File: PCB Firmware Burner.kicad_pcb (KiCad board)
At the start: 2 copper layers, 34.7 x 35.3 mm, 19 parts, among them J1 Conn_01x06_Male, Q1 BSS138, Q2 BSS138

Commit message: revision 1.1
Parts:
- removed CHC1: 100nF, Capacitor_SMD:C_1206_3216Metric
- removed the REF** at (159.0, 75.6)
- removed the REF** at (167.5, 75.5)
- added G***: LOGO, AeonLabs:aeon creative commons logos, F.Cu at (175.6, 99.8)
- added G***: LOGO, AeonLabs:aeon creative commons logos, B.Cu at (163.5, 98.1)
- added QR1: 10K, Resistor_SMD:R_0805_2012Metric_Pad1.20x1.40mm_HandSolder, F.Cu at (168.3, 88.8)
- added QR2: 10K, Resistor_SMD:R_0805_2012Metric_Pad1.20x1.40mm_HandSolder, F.Cu at (174.1, 90.6)
- added REF**: TestPoint_Plated_Hole_D2.0mm, TestPoint:TestPoint_Plated_Hole_D2.0mm, F.Cu at (160.7, 75.4)
- added REF**: TestPoint_Plated_Hole_D2.0mm, TestPoint:TestPoint_Plated_Hole_D2.0mm, F.Cu at (167.1, 75.5)
- moved Q2 2.60 mm to (176.9, 88.5)
- moved Q1 2.36 mm to (171.1, 88.0)
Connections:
- CH340K1 pad 4: Net-(Q2-Pad1) -> Net-(CH340K1-Pad4)
- CH340K1 pad 6: Net-(Q2-Pad2) -> Net-(CH340K1-Pad6)
- LDR1 pad 1: /CH3V3 -> /3V3
- Q1 pad 1: Net-(Q2-Pad2) -> Net-(Q1-Pad1)
- Q1 pad 2: Net-(Q2-Pad1) -> Net-(CH340K1-Pad4)
- Q2 pad 2: Net-(Q2-Pad2) -> Net-(CH340K1-Pad6)
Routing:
- net Net-(CH340K1-Pad6): track 0.00 -> 16.6 mm, vias 0 -> 4
- net Net-(Q2-Pad2): track 16.4 -> 0.00 mm, vias 3 -> 0
- net /GND: track 89.3 -> 78.2 mm
- net Net-(Q2-Pad1): track 10.8 -> 1.93 mm
- net Net-(CH340K1-Pad4): track 0.00 -> 8.34 mm
- net /RST_EN_RTS: track 15.8 -> 10.6 mm
- net Net-(Q1-Pad1): track 0.00 -> 2.31 mm
- net /IO0_BOOT_DTR: track 5.69 -> 6.94 mm
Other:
- board text added: "3V3"
- board text added: "Copyright 2022 rev. 1.1"
- board text removed: "Copyright 2022 rev. 1.0"

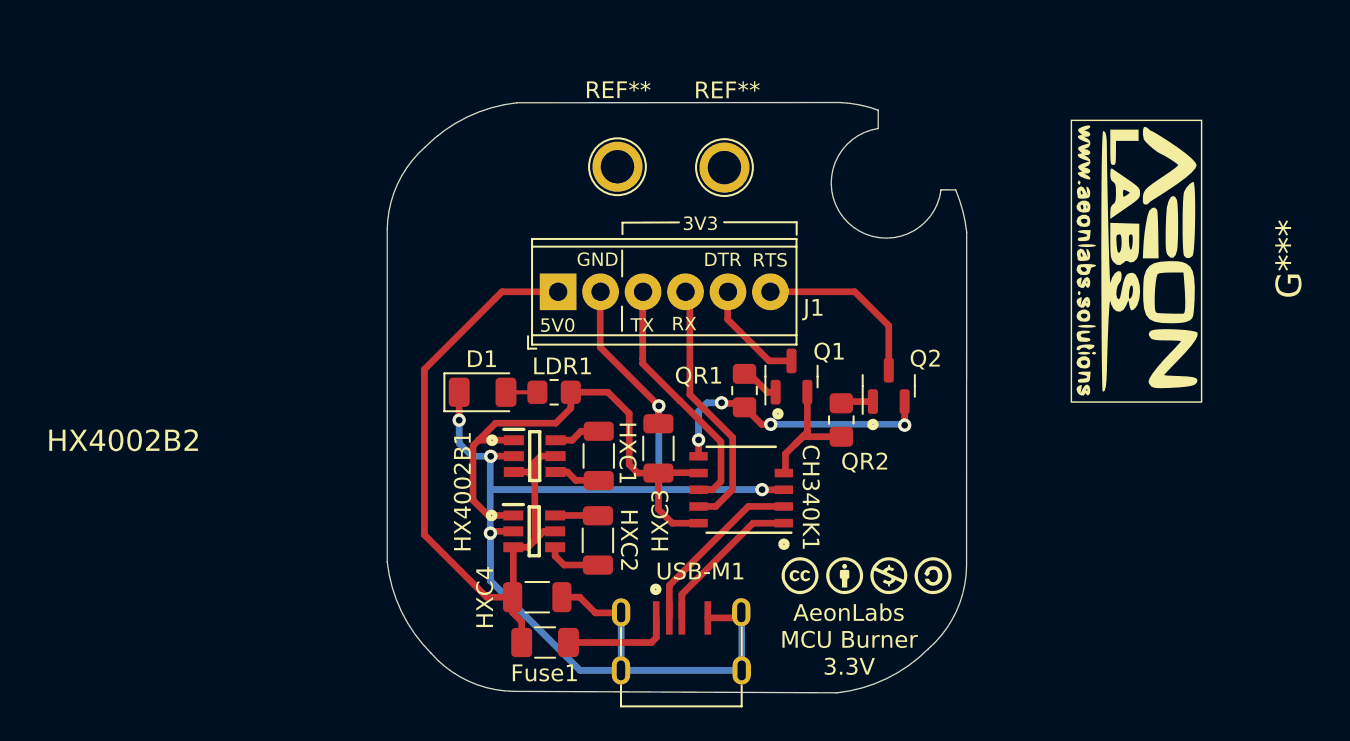
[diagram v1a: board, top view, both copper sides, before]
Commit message: revision 1.2
possibility of voltage selection: 3V3 or 5V0
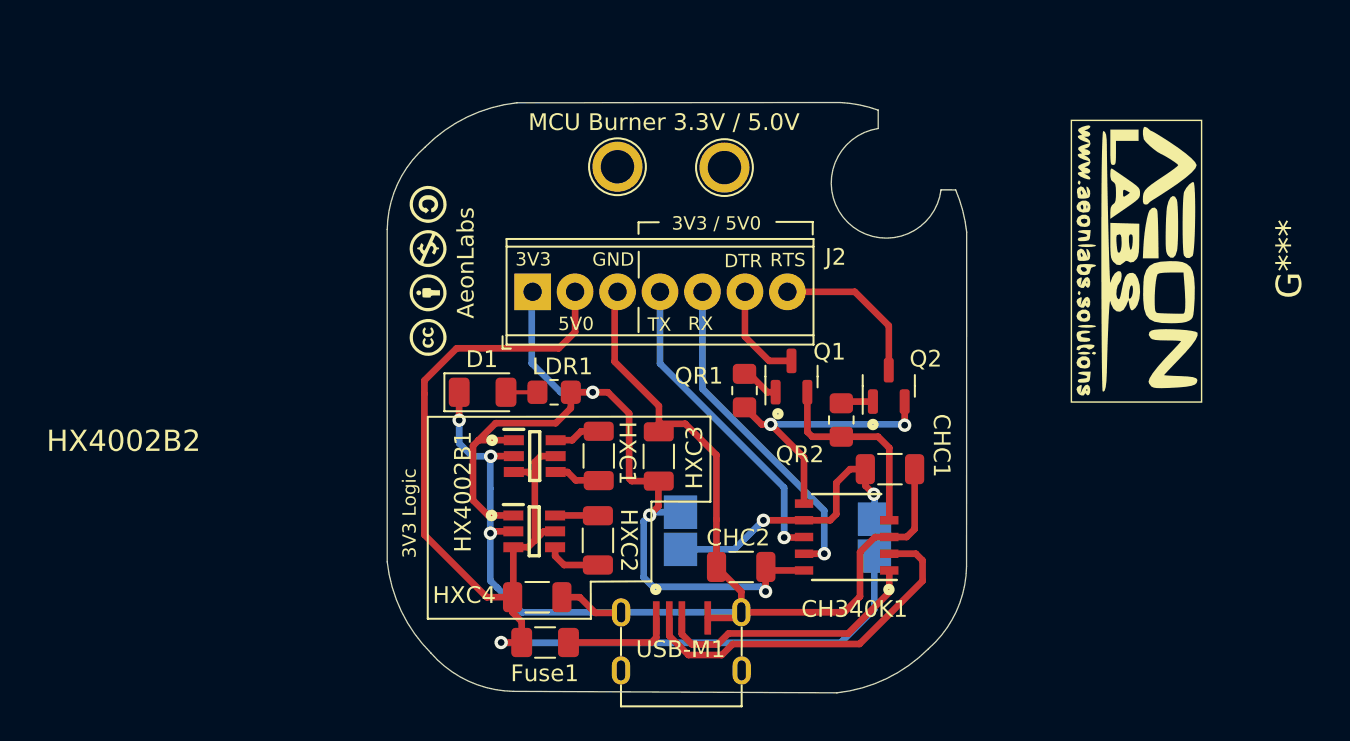
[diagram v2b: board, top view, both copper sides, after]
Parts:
- removed J1: Conn_01x06_Male, TerminalBlock_Phoenix:TerminalBlock_Phoenix_MPT-0,5-6-2.54_1x06_P2.54mm_Horizontal
- added CHC1: 100nF, Capacitor_SMD:C_1206_3216Metric, F.Cu at (177.0, 93.5)
- added CHC2: 100nF, Capacitor_SMD:C_1206_3216Metric, F.Cu at (168.1, 99.3)
- added J2: Conn_01x07_Male, TerminalBlock_Phoenix:TerminalBlock_Phoenix_MPT-0,5-7-2.54_1x07_P2.54mm_Horizontal, F.Cu at (155.6, 82.9)
- added T5V0b1: T5V0b1, TestPoint:TestPoint_Pad_2.0x2.0mm, B.Cu at (176.1, 98.7)
- added T5V0b2: T5V0b2, TestPoint:TestPoint_Pad_2.0x2.0mm, B.Cu at (164.5, 98.3)
- added T5V0c1: T5V0c1, TestPoint:TestPoint_Pad_2.0x2.0mm, B.Cu at (176.1, 96.5)
- added T5V0c2: T5V0c2, TestPoint:TestPoint_Pad_2.0x2.0mm, B.Cu at (164.5, 96.1)
- moved G*** 31.9 mm to (149.3, 81.7), turned to 90 degrees
- moved G*** 19.7 mm to (164.1, 78.4)
- moved CH340K1 6.91 mm to (174.4, 97.6)
- moved HXC3 0.48 mm to (163.2, 92.7)
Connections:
- CH340K1 pad 10: /CH3V3 -> /HX3V3
- CH340K1 pad 7: /CH3V3 -> Net-(CH340K1-Pad7)
- HX4002B1 pad 1: /CH3V3 -> /HX3V3
- HX4002B2 pad 1: /CH3V3 -> /HX3V3
- HXC3 pad 1: /CH3V3 -> /HX3V3
- LDR1 pad 1: /3V3 -> /HX3V3
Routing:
- net /HX3V3: track 0.00 -> 54.1 mm, vias 0 -> 3
- net /CH3V3: track 33.1 -> 0.00 mm
- net /5V0: track 42.8 -> 72.4 mm, vias 0 -> 1
- net Net-(CH340K1-Pad7): track 0.00 -> 17.4 mm, vias 0 -> 2
- net Net-(CH340K1-Pad2): track 10.7 -> 21.9 mm
- net Net-(CH340K1-Pad1): track 9.27 -> 16.2 mm
- net /RX_OUT_3V3: track 15.9 -> 20.1 mm, vias 0 -> 1
- net /TX_OUT_3V3: track 15.3 -> 19.2 mm, vias 0 -> 1
- net Net-(CH340K1-Pad4): track 8.34 -> 12.0 mm
- net /RST_EN_RTS: track 10.6 -> 9.57 mm
- net /IO0_BOOT_DTR: track 6.94 -> 6.07 mm
- net Net-(CH340K1-Pad6): track 16.6 -> 17.0 mm, vias 4 -> 2
- net /GND: track 78.2 -> 78.3 mm, vias 5 -> 3
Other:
- board text added: "3V3 / 5V0"
- board text added: "3V3 Logic"
- board text added: "AeonLabs"
- board text added: "Copyright 2022 rev. 1.2"
- board text added: "EN 3V0"
- board text added: "EN 5V0"
- board text added: "MCU Burner 3.3V / 5.0V"
- board text removed: "AeonLabs MCU Burner 3.3V"
- board text removed: "Copyright 2022 rev. 1.1"

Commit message: revision 1,3
Track bug corrections
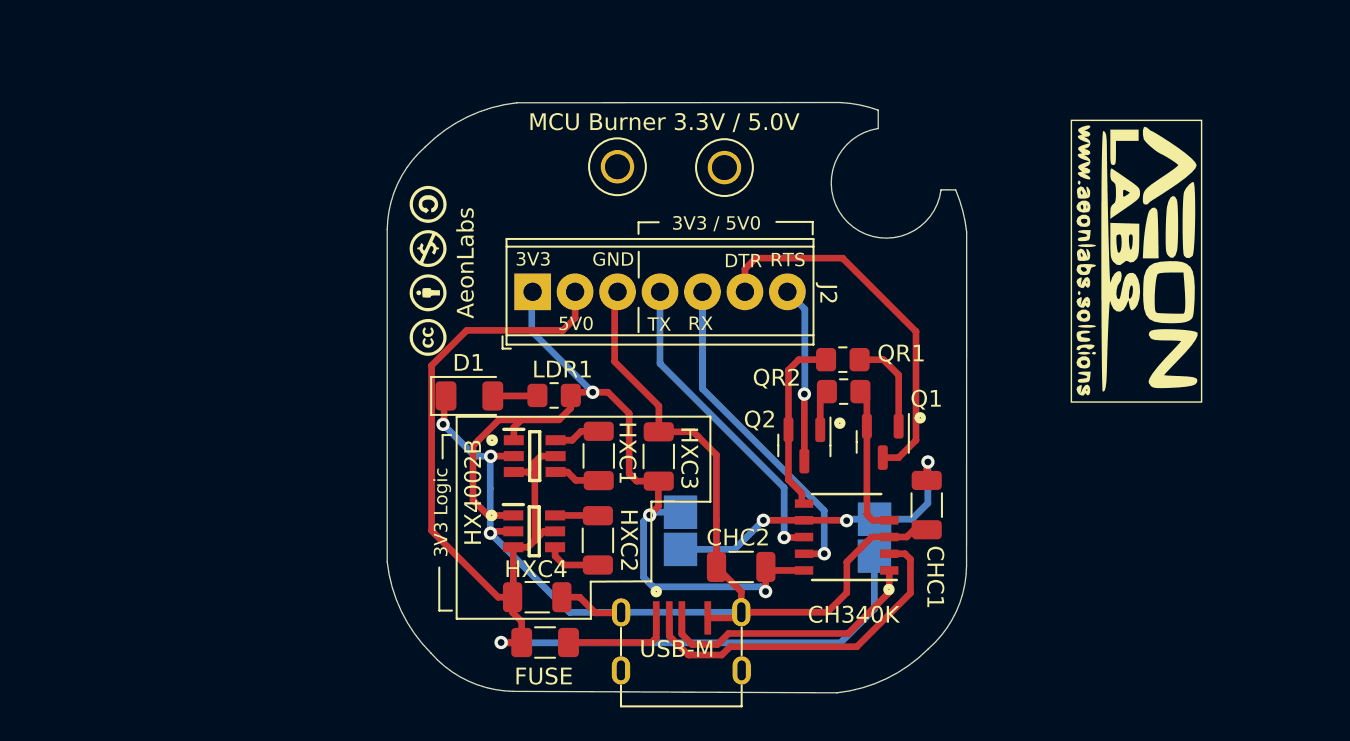
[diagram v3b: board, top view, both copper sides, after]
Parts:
- moved Q1 6.72 mm to (176.6, 91.9), turned to -90 degrees
- moved Q2 6.18 mm to (171.9, 92.1), turned to -90 degrees
- moved QR1 6.16 mm to (174.2, 87.0), turned to 0 degrees
- moved CHC1 3.08 mm to (179.2, 95.7), turned to -90 degrees
- moved QR2 1.71 mm to (174.2, 88.9), turned to 180 degrees
- moved D1 0.82 mm to (151.8, 89.1)
- moved LDR1 0.19 mm to (156.9, 89.1)
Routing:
- net /IO0_BOOT_DTR: track 6.07 -> 22.6 mm
- net Net-(CH340K1-Pad6): track 17.0 -> 10.9 mm, vias 2 -> 0
- net /GND: track 78.3 -> 72.4 mm
- net Net-(Q1-Pad1): track 2.31 -> 5.78 mm
- net Net-(CH340K1-Pad4): track 12.0 -> 9.00 mm
- net Net-(CH340K1-Pad7): track 17.4 -> 19.6 mm, vias 2 -> 3
- net /HX3V3: track 54.1 -> 52.1 mm
- net /RST_EN_RTS: track 9.57 -> 10.6 mm, vias 0 -> 1
- net Net-(CH340K1-Pad2): track 21.9 -> 20.9 mm
- net /5V0: track 72.4 -> 71.5 mm
- net Net-(D1-Pad2): track 1.88 -> 2.76 mm
- net Net-(Q2-Pad1): track 1.93 -> 2.59 mm
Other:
- board text added: "CH340K"
- board text added: "Copyright 2022 rev. 1.3"
- board text added: "FUSE"
- board text added: "HX4002B"
- board text added: "USB-M"
- board text removed: "Copyright 2022 rev. 1.2"

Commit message: rev 1.4
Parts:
- removed REF** (x2): TestPoint_Plated_Hole_D2.0mm, TestPoint:TestPoint_Plated_Hole_D2.0mm
- added TP3: TP_3Pole, TestPoint:TestPoint_Pad_1.5mm 3 points, F.Cu at (172.9, 100.9)
- added TP4: TP_3Pole, TestPoint:TestPoint_Pad_1.5mm 3 points, F.Cu at (178.2, 100.9)
- J2: footprint TerminalBlock_Phoenix:TerminalBlock_Phoenix_MPT-0,5-7-2.54_1x07_P2.54mm_Horizontal -> Connector_PinHeader_2.54mm:PinHeader_1x07_P2.54mm_Horizontal
- moved G*** 12.8 mm to (163.9, 91.2)
- moved QR1 5.30 mm to (176.5, 82.2)
- moved BSS 5.30 mm to (174.2, 87.3)
- moved Q1 5.30 mm to (178.9, 87.1)
- moved QR2 5.30 mm to (176.5, 84.1)
- moved CH340K1 4.48 mm to (175.5, 93.2)
- moved CHC1 4.48 mm to (180.2, 91.3)
- moved T5V0b1 4.48 mm to (177.1, 94.3)
- moved T5V0c1 4.48 mm to (177.1, 92.1)
- moved G*** 3.85 mm to (163.5, 85.1)
- moved J2 3.08 mm to (155.6, 79.8), turned to 90 degrees
- moved G*** 0.95 mm to (148.4, 81.9)
- renumbered Q2 to BSS
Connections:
- USB-M1 pad 2: Net-(CH340K1-Pad2) -> Net-(TP4-Pad1)
- USB-M1 pad 3: Net-(CH340K1-Pad1) -> Net-(TP3-Pad1)
- USB-M1 pad 6: /GND -> unconnected-(USB-M1-Pad6)
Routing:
- net Net-(TP4-Pad1): track 0.00 -> 19.1 mm
- net Net-(CH340K1-Pad2): track 20.9 -> 6.70 mm
- net Net-(TP3-Pad1): track 0.00 -> 13.5 mm
- net /HX3V3: track 52.1 -> 62.9 mm, vias 3 -> 4
- net /5V0: track 71.5 -> 81.9 mm
- net Net-(CH340K1-Pad1): track 16.2 -> 6.64 mm
- net /TX_OUT_3V3: track 19.2 -> 26.5 mm, vias 1 -> 3
- net /RX_OUT_3V3: track 20.1 -> 25.2 mm, vias 1 -> 2
- net Net-(CH340K1-Pad7): track 19.6 -> 22.6 mm
- net /GND: track 72.4 -> 71.4 mm, vias 3 -> 4
- net Net-(CH340K1-Pad4): track 9.00 -> 8.01 mm
- net Net-(Q2-Pad1): track 2.59 -> 1.82 mm
- net /RST_EN_RTS: track 10.6 -> 9.96 mm
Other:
- board text added: "3V0"
- board text added: "3V3/5V0"
- board text added: "Copyright 2022"
- board text added: "D+"
- board text added: "D-"
- board text added: "SELECTION"
- board text added: "URT"
- board text added: "USB"
- board text added: "rev. 1.4"
- board text removed: "3V3 / 5V0"
- board text removed: "Copyright 2022 rev. 1.3"
- board text removed: "EN 3V0"
- board text removed: "EN 5V0"

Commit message: update
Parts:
- removed BSS: BSS138, Package_TO_SOT_SMD:SOT-23
- removed the G*** at (191.8, 81.1)
- added Q2: BSS138, Package_TO_SOT_SMD:SOT-23, F.Cu at (174.2, 87.0)
- moved TP4 20.9 mm to (163.7, 85.9), turned to -90 degrees
- moved TP3 15.6 mm to (169.3, 85.8), turned to -90 degrees
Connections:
- CH340K1 pad 1: Net-(CH340K1-Pad1) -> Net-(USB-M1-Pad3)
- CH340K1 pad 8: /TX_OUT_3V3 -> Net-(CH340K1-Pad8)
- CH340K1 pad 9: /RX_OUT_3V3 -> Net-(CH340K1-Pad9)
- TP3 pad 1: Net-(TP3-Pad1) -> /RX_OUT_3V3
- TP3 pad 2: Net-(CH340K1-Pad1) -> Net-(CH340K1-Pad9)
- TP3 pad 3: /TX_OUT_3V3 -> Net-(CH340K1-Pad2)
- TP4 pad 1: Net-(TP4-Pad1) -> /TX_OUT_3V3
- TP4 pad 2: Net-(CH340K1-Pad2) -> Net-(CH340K1-Pad8)
- TP4 pad 3: /RX_OUT_3V3 -> Net-(USB-M1-Pad3)
- USB-M1 pad 2: Net-(TP4-Pad1) -> Net-(CH340K1-Pad2)
- USB-M1 pad 3: Net-(TP3-Pad1) -> Net-(USB-M1-Pad3)
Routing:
- net Net-(USB-M1-Pad3): track 0.00 -> 35.3 mm, vias 0 -> 2
- net Net-(CH340K1-Pad2): track 6.70 -> 38.3 mm, vias 0 -> 2
- net /TX_OUT_3V3: track 26.5 -> 5.41 mm, vias 3 -> 0
- net Net-(TP4-Pad1): track 19.1 -> 0.00 mm
- net /RX_OUT_3V3: track 25.2 -> 6.62 mm, vias 2 -> 0
- net Net-(CH340K1-Pad8): track 0.00 -> 14.5 mm, vias 0 -> 1
- net Net-(TP3-Pad1): track 13.5 -> 0.00 mm
- net Net-(CH340K1-Pad9): track 0.00 -> 10.9 mm, vias 0 -> 2
- net Net-(CH340K1-Pad1): track 6.64 -> 0.00 mm
- net Net-(CH340K1-Pad7): track 22.6 -> 25.6 mm
- net /IO0_BOOT_DTR: track 22.9 -> 21.8 mm
- net /GND: track 71.4 -> 72.1 mm
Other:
- board text removed: "LDAD NANO 1x HXG/HXW 1x DS/I2C/LS"
- board text removed: "PLUG 1"
